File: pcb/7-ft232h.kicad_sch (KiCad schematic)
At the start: 0 parts

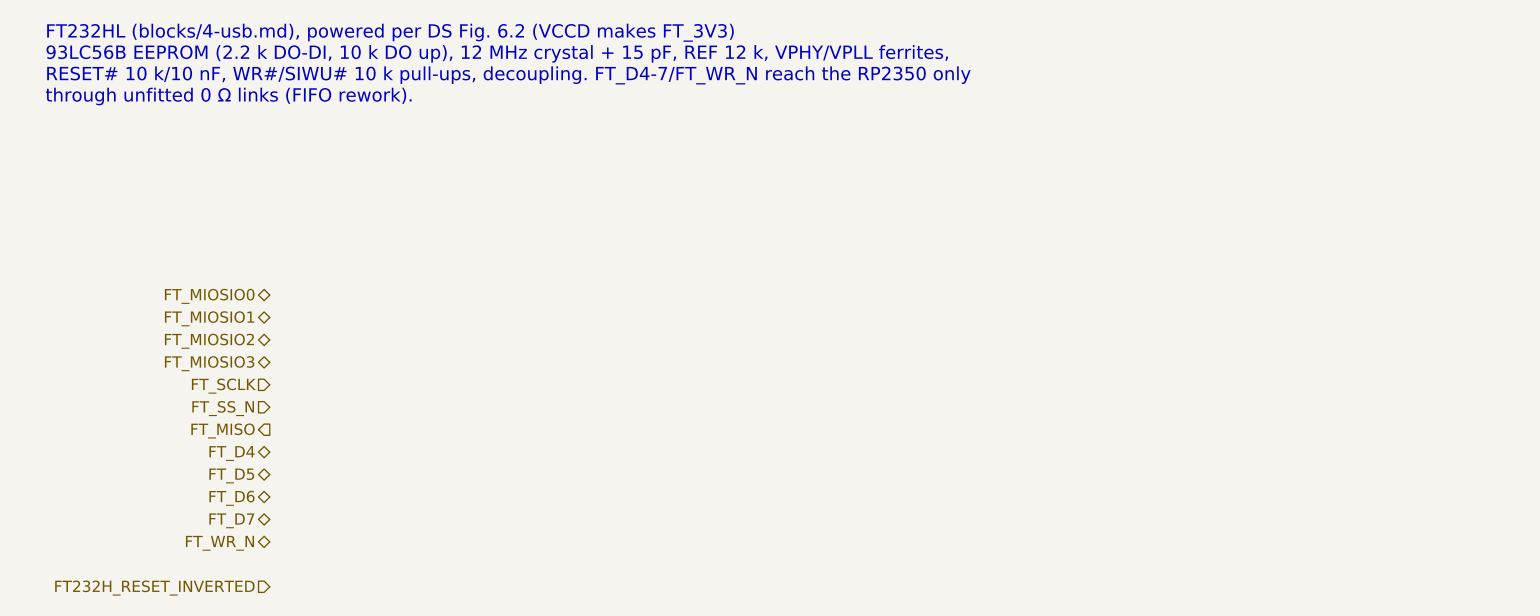
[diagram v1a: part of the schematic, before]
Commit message: Phase 3: populate RP2350 sheet; FT_* nets renamed FT232H_*
RP2350 sheet (A2): RP2350B with every pin labelled by function and the
FT1248, marker and USB series resistors inline on their pins; core
regulator, per-pin decoupling (14 x 100 nF, count corrected), crystal,
QSPI flash and PSRAM in separate boxes, TC2030 debug pads and buttons,
the FT1248 rework links, and the TERMPWR sense divider on ADC6.

Generator: recursive derived-symbol flattening, small field fonts.
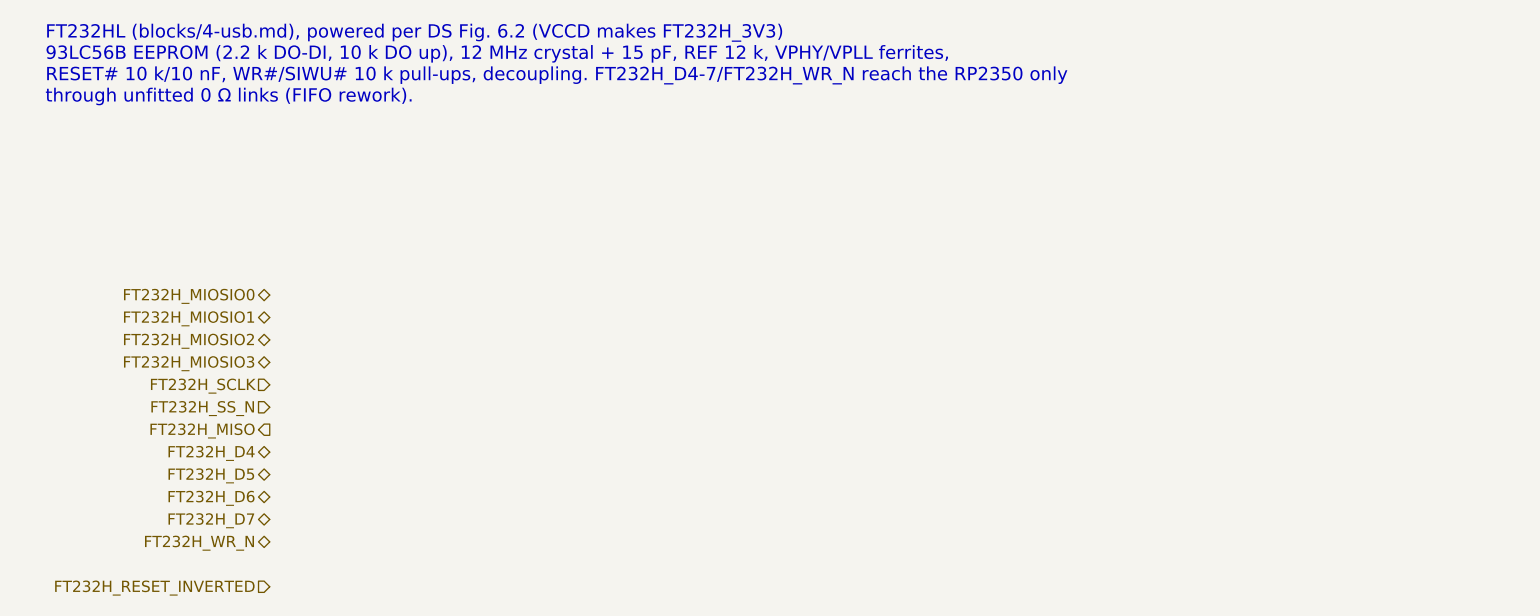
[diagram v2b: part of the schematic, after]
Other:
- note added: "FT232HL (blocks/4-usb.md), powered per DS Fig. 6.2 (VCCD makes FT232H_3V3) 93LC56B EEPROM (2.2 k DO-DI, 10 k DO up), 12 MHz crystal + 15 pF, REF 12 k, VPHY/VPLL ferrites, RESET# 10 k/10 nF, WR#/SIWU# 10 k pull-ups, decoupling. FT232H_D4-7/FT232H_WR_N reach the RP2350 only through unfitted 0 Ω links (FIFO rework)."
- note removed: "FT232HL (blocks/4-usb.md), powered per DS Fig. 6.2 (VCCD makes FT_3V3) 93LC56B EEPROM (2.2 k DO-DI, 10 k DO up), 12 MHz crystal + 15 pF, REF 12 k, VPHY/VPLL ferrites, RESET# 10 k/10 nF, WR#/SIWU# 10 k pull-ups, decoupling. FT_D4-7/FT_WR_N reach the RP2350 only through unfitted 0 Ω links (FIFO rework)."
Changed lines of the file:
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@@
 		(rev "0.1")
 	)
-	(text "FT232HL (blocks/4-usb.md), powered per DS Fig. 6.2 (VCCD makes FT_3V3)\n93LC56B EEPROM (2.2 k DO-DI, 10 k DO up), 12 MHz crystal + 15 pF, REF 12 k, VPHY/VPLL ferrites,\nRESET# 10 k/10 nF, WR#/SIWU# 10 k pull-ups, decoupling. FT_D4-7/FT_WR_N reach the RP2350 only\nthrough unfitted 0 Ω links (FIFO rework)."
+	(text "FT232HL (blocks/4-usb.md), powered per DS Fig. 6.2 (VCCD makes FT232H_3V3)\n93LC56B EEPROM (2.2 k DO-DI, 10 k DO up), 12 MHz crystal + 15 pF, REF 12 k, VPHY/VPLL ferrites,\nRESET# 10 k/10 nF, WR#/SIWU# 10 k pull-ups, decoupling. FT232H_D4-7/FT232H_WR_N reach the RP2350 only\nthrough unfitted 0 Ω links (FIFO rework)."
 		(exclude_from_sim no)
 		(at 25.4 20.32 0)
@@
 		)
 	)
-	(hierarchical_label "FT_D6"
+	(hierarchical_label "FT232H_D6"
 		(shape bidirectional)
 		(at 50.8 73.66 180)
@@
 		)
 	)
-	(hierarchical_label "FT_SCLK"
+	(hierarchical_label "FT232H_SCLK"
 		(shape input)
 		(at 50.8 60.96 180)
@@
 		)
 	)
-	(hierarchical_label "FT_MIOSIO3"
+	(hierarchical_label "FT232H_MIOSIO3"
 		(shape bidirectional)
 		(at 50.8 58.42 180)
@@
 		)
 	)
-	(hierarchical_label "FT_MISO"
+	(hierarchical_label "FT232H_MISO"
 		(shape output)
 		(at 50.8 66.04 180)
@@
 		)
 	)
-	(hierarchical_label "FT_MIOSIO1"
+	(hierarchical_label "FT232H_MIOSIO1"
 		(shape bidirectional)
 		(at 50.8 53.34 180)
@@
 		)
 	)
-	(hierarchical_label "FT_SS_N"
+	(hierarchical_label "FT232H_SS_N"
 		(shape input)
 		(at 50.8 63.5 180)
@@
 		)
 	)
-	(hierarchical_label "FT_WR_N"
+	(hierarchical_label "FT232H_WR_N"
 		(shape bidirectional)
 		(at 50.8 78.74 180)
@@
 		)
 	)
-	(hierarchical_label "FT_D7"
+	(hierarchical_label "FT232H_D7"
 		(shape bidirectional)
 		(at 50.8 76.2 180)
@@
 		)
 	)
-	(hierarchical_label "FT_MIOSIO2"
+	(hierarchical_label "FT232H_MIOSIO2"
 		(shape bidirectional)
 		(at 50.8 55.88 180)
@@
 		)
 	)
-	(hierarchical_label "FT_MIOSIO0"
+	(hierarchical_label "FT232H_MIOSIO0"
 		(shape bidirectional)
 		(at 50.8 50.8 180)
@@
 		)
 	)
-	(hierarchical_label "FT_D4"
+	(hierarchical_label "FT232H_D4"
 		(shape bidirectional)
 		(at 50.8 68.58 180)
@@
 		)
 	)
-	(hierarchical_label "FT_D5"
+	(hierarchical_label "FT232H_D5"
 		(shape bidirectional)
 		(at 50.8 71.12 180)

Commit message: Phase 3: populate FT232H sheet; FT232H_WR_N -> FT232H_WRITE_INVERTED
FT232HL per DS Fig. 6.2 (VCCD makes FT232H_3V3), ferrite-fed VPHY/VPLL,
93LC56B config EEPROM, crystal, REF, RESET RC and FIFO-fallback pull-ups.
Project FT232H symbol retypes EECS/EECLK as outputs (and VCCD as
power_out); upstream fix recorded as a follow-up (NOTES open question 14).
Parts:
- added C701, C703: 4.7uF 10V, Capacitor_SMD:C_0402_1005Metric, symbol Device:C
- added C702, C704, C705, C706, C707, C708, C710, C712, C713, C714: 100nF, Capacitor_SMD:C_0402_1005Metric, symbol Device:C
- added C709, C711: 4.7uF, Capacitor_SMD:C_0402_1005Metric, symbol Device:C
- added C715, C716: 15pF, Capacitor_SMD:C_0402_1005Metric, symbol Device:C
- added C717: 10nF, Capacitor_SMD:C_0402_1005Metric, symbol Device:C
- added FB701, FB702: 600R@100MHz, Inductor_SMD:L_0603_1608Metric, symbol Device:FerriteBead_Small
- added R701: 12k 1%, Resistor_SMD:R_0402_1005Metric, symbol Device:R
- added R702, R703, R705, R706: 10k, Resistor_SMD:R_0402_1005Metric, symbol Device:R
- added R704: 2.2k, Resistor_SMD:R_0402_1005Metric, symbol Device:R
- added TP701: FT232H_3V3, TestPoint:TestPoint_Pad_D1.5mm, symbol Connector:TestPoint
- added U701: FT232HL, Package_QFP:LQFP-48_7x7mm_P0.5mm, symbol scsi-adapter:FT232H
- added U702: 93LC56BT-I/OT, Package_TO_SOT_SMD:SOT-23-6, symbol Memory_EEPROM:93LCxxBxxOT
- added Y701: 12MHz ABM8-272-T3, Crystal:Crystal_SMD_3225-4Pin_3.2x2.5mm, symbol Device:Crystal_GND24
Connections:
- net FT232H_D4: now also U701.17 (ADBUS4)
- net FT232H_D5: now also U701.18 (ADBUS5)
- net FT232H_D6: now also U701.19 (ADBUS6)
- net FT232H_D7: now also U701.20 (ADBUS7)
- net FT232H_MIOSIO0: now also U701.13 (ADBUS0)
- net FT232H_MIOSIO1: now also U701.14 (ADBUS1)
- net FT232H_MIOSIO2: now also U701.15 (ADBUS2)
- net FT232H_MIOSIO3: now also U701.16 (ADBUS3)
- net FT232H_MISO: now also U701.26 (ACBUS2)
- net FT232H_RESET_INVERTED: now also C717.1, R702.2, U701.34 (~{RESET})
- net FT232H_SCLK: now also U701.21 (ACBUS0)
- net FT232H_SS_N: now also U701.25 (ACBUS1)
- net USB_FT_D+: now also U701.7 (DP)
- net USB_FT_D-: now also U701.6 (DM)
- new net +5V_SYS: C701.1, C702.1, U701.40 (VREGIN)
- new net FT232H_3V3: C703.1, C704.1, C705.1, C706.1, C707.1, C714.1, FB701.1, FB702.1, R702.1, R703.1, R705.1, R706.1, TP701.1, U701.12 (VCCIO), U701.24 (VCCIO), U701.39 (VCCD), U701.46 (VCCIO), U702.6 (VCC)
- new net FT232H_EECLK: U701.44 (EECLK), U702.4 (CLK)
- new net FT232H_EECS: U701.45 (EECS), U702.5 (CS)
- new net FT232H_EEDATA: R704.2, U701.43 (EEDATA), U702.3 (DI)
- new net FT232H_EEPROM_DO: R703.2, R704.1, U702.1 (DO)
- new net FT232H_REF: R701.1, U701.5 (REF)
- new net FT232H_SIWU_N: R706.2, U701.28 (ACBUS4)
- new net FT232H_VCCA: C712.1, U701.37 (VCCA)
- new net FT232H_VCORE: C713.1, U701.38 (VCCCORE)
- new net FT232H_VPHY: C708.1, C709.1, FB701.2, U701.3 (VPHY)
- new net FT232H_VPLL: C710.1, C711.1, FB702.2, U701.8 (VPLL)
- new net FT232H_WRITE_INVERTED: R705.2, U701.27 (ACBUS3)
- new net FT232H_XCSI: C715.1, U701.1 (XCSI), Y701.1
- new net FT232H_XCSO: C716.1, U701.2 (XCSO), Y701.3
- new net GND: C701.2, C702.2, C703.2, C704.2, C705.2, C706.2, C707.2, C708.2, C709.2, C710.2, C711.2, C712.2, C713.2, C714.2, C715.2, C716.2, C717.2, R701.2, U701.10 (GND), U701.11 (GND), U701.22 (GND), U701.23 (GND), U701.35 (GND), U701.36 (GND), U701.4 (AGND), U701.41 (AGND), U701.42 (TEST), U701.47 (GND), U701.48 (GND), U701.9 (AGND), U702.2 (GND), Y701.2 (G), Y701.4 (G)
- no-connect marks 0 -> 5
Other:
- note added: "12 MHz crystal (same ABM8 as the RP2350 and hub) with 2 x 15 pF; REF 12k 1 % (DS Table 3.2); RESET# 10k + 10 nF (the expander's P13 can also pull it low); WR#/SIWU# pull-ups for the FIFO fallback."
- note added: "ACBUS5/6/8/9: free (CBUS bit-bang possible later). ACBUS7 = PWRSAV#: leave open, with 'Suspend on ACBus7 Low' OFF in the EEPROM. TEST (42) to GND."
- note added: "Configuration EEPROM (93LC56B, required)"
- note added: "EEDATA drives DI directly and reads DO through R704 (DS Table 3.3; the figure shows 2k)."
- note added: "FT1248 4-bit to the RP2350 (MIOSIO0-3, SCLK, SS_N, MISO; 33R series at the RP2350 end). The EEPROM selects FT1248 mode: without it the chip starts in UART mode. D4-D7 and WR# only reach the RP2350 through the unfitted rework links (245-FIFO fallback). SCLK/SS_N/MISO sit on the FIFO's RXF#/TXE#/RD# pins."
- note added: "FT232H (USB 2.0 high speed <-> FT1248)"
- note added: "Holds FT1248 mode. Programmed over USB after assembly (USAGE.md). The 93LC46B won't work."
- note added: "PWR_FLAGs: VPHY and VPLL are fed through ferrites (passive to ERC). U701 is a project copy of KiCad's FT232H with VCCD, EECS, EECLK typed as outputs. C709/C711 DNP: 4.7 uF pads per FTDI, fit if the PHY/PLL rails need more bulk."
- note added: "Power (DS Fig. 6.2, exactly)"
- note added: "Support parts"
- note added: "VREGIN from +5V_SYS. VCCD is then an OUTPUT: the chip's own 3.3 V (FT232H_3V3), feeding VCCIO x3, VPHY and VPLL (through 600R ferrites) and the EEPROM. Never connect FT232H_3V3 to the board's +3V3."
- note added: "WR# (27) and SIWU# (28) are pulled up so the 245-FIFO fallback never floats them; harmless in FT1248 mode."
- note removed: "FT232HL (blocks/4-usb.md), powered per DS Fig. 6.2 (VCCD makes FT232H_3V3) 93LC56B EEPROM (2.2 k DO-DI, 10 k DO up), 12 MHz crystal + 15 pF, REF 12 k, VPHY/VPLL ferrites, RESET# 10 k/10 nF, WR#/SIWU# 10 k pull-ups, decoupling. FT232H_D4-7/FT232H_WR_N reach the RP2350 only through unfitted 0 Ω links (FIFO rework)."
